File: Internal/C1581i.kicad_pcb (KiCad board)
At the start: 2 copper layers, 151.5 x 106.9 mm, 71 parts, among them CN1 FLOPPY POWER, CN2 FLOPPY, CN5 LEDS, CN7 INTERNAL IEC, CN8 EXTERNAL POWER, J1 PIN34, J2 PIN2, J3 DRIVE SELECT, J5 ROM SELECT, J90 Barrel_Jack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

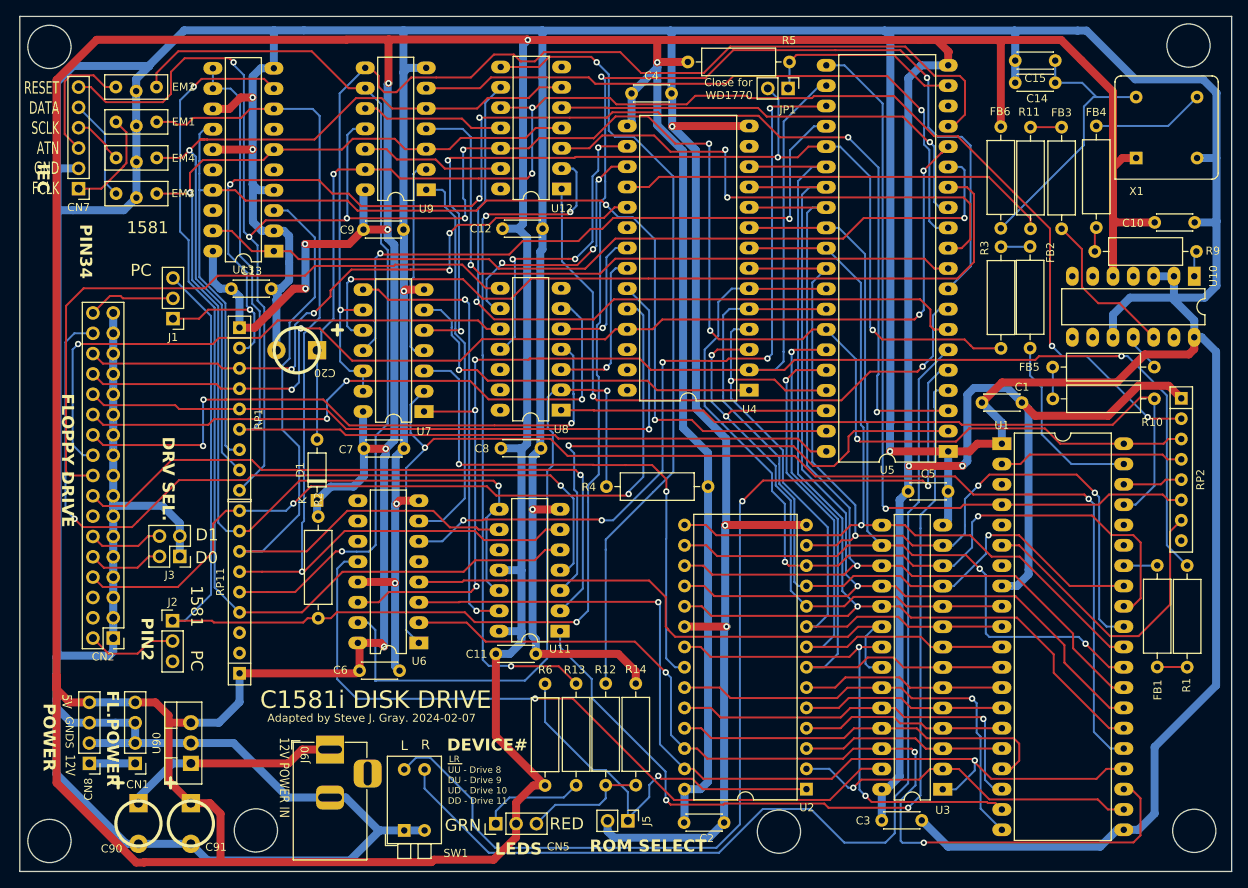
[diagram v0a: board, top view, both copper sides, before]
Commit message: 1581i Update
Lots of re-routing to pack components tighter. PCB is now smaller. Added FPC connector to add Laptop PC drive support. Add board render.
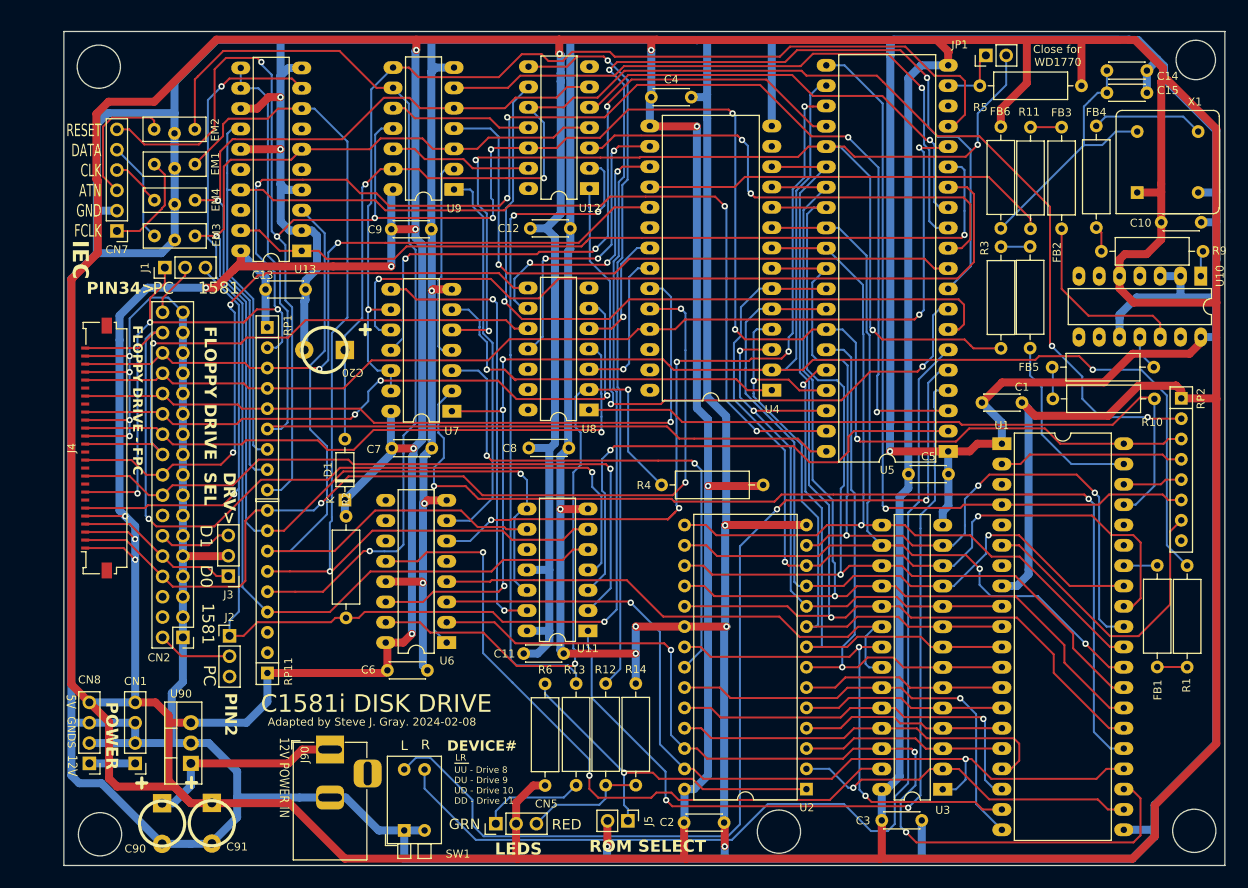
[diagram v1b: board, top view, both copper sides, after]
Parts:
- added J4: Conn_01x26, Connector_FFC-FPC:Molex_200528-0260_1x26-1MP_P1.00mm_Horizontal, F.Cu at (96.7, 89.9)
- J3: value DRIVE SELECT -> PIN2; footprint Connector_PinHeader_2.54mm:PinHeader_2x02_P2.54mm_Vertical -> Connector_PinHeader_2.54mm:PinHeader_1x03_P2.54mm_Vertical
- moved JP1 25.1 mm to (208.3, 40.8), turned to 90 degrees
- moved R5 24.0 mm to (207.6, 44.6), turned to 0 degrees
- moved CN2 8.71 mm to (108.0, 113.5)
- moved C15 7.61 mm to (223.5, 45.5), turned to 0 degrees
- moved J2 7.37 mm to (113.8, 113.3)
- moved CN7 7.14 mm to (99.7, 62.7)
- moved EM1 7.14 mm to (109.5, 54.4)
- moved EM4 7.14 mm to (109.5, 58.9)
- moved EM2 7.14 mm to (109.5, 50.0)
- moved EM3 7.14 mm to (109.5, 63.4)
- moved R4 6.89 mm to (167.8, 94.5)
- moved C14 6.64 mm to (223.5, 42.7), turned to 0 degrees
- moved J3 6.55 mm to (113.7, 105.9)
- moved J1 6.47 mm to (105.7, 67.3), turned to 90 degrees
- moved X1 4.31 mm to (227.3, 57.9)
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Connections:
- J3 pad 1: GND -> SELECT0
- J3 pad 2: SELECT0 -> GND
- J3 pad 3: GND -> SELECT1
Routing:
- net 5V: track 960.5 -> 1196.3 mm, vias 10 -> 13
- net GND: track 1108.0 -> 1220.9 mm, vias 10 -> 17
- net ~{RDY}: track 169.5 -> 212.8 mm, vias 6 -> 8
- net PHI2: track 127.3 -> 147.3 mm
- net Net-(JP1-A): track 25.2 -> 8.08 mm
- net ~{DISKCHANGE}: track 244.7 -> 261.7 mm, vias 3 -> 4
- net INDEX: track 100.8 -> 115.1 mm, vias 2 -> 3
- net SELECT0: track 9.47 -> 20.6 mm
- net Net-(R12-Pad2): track 99.3 -> 91.0 mm
- net ATN_IN: track 137.7 -> 130.2 mm
- net A3: track 74.7 -> 68.5 mm
- net READDATA: track 82.3 -> 88.3 mm, vias 4 -> 2
- net A14: track 116.5 -> 110.6 mm
- net SIDE0: track 70.9 -> 65.0 mm
- net ~{FLAG}: track 80.6 -> 86.4 mm, vias 2 -> 3
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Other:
- board size 151.5 x 106.9 mm -> 145.1 x 104.2 mm
- board text added: "Adapted by Steve J. Gray. 2024-02-08"
- board text added: "DRV> SEL"
- board text added: "FLOPPY DRIVE - FPC"
- board text added: "PIN34>"
- board text added: "RESET DATA CLK ATN GND FCLK"
- board text removed: "Adapted by Steve J. Gray. 2024-02-07"
- board text removed: "DRV SEL."
- board text removed: "FL.POWER"
- board text removed: "PIN34"
- board text removed: "RESET DATA SCLK ATN GND FCLK"

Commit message: Floppy connector area updates
Move floppy connector and jumpers. Add additional mounting holes.
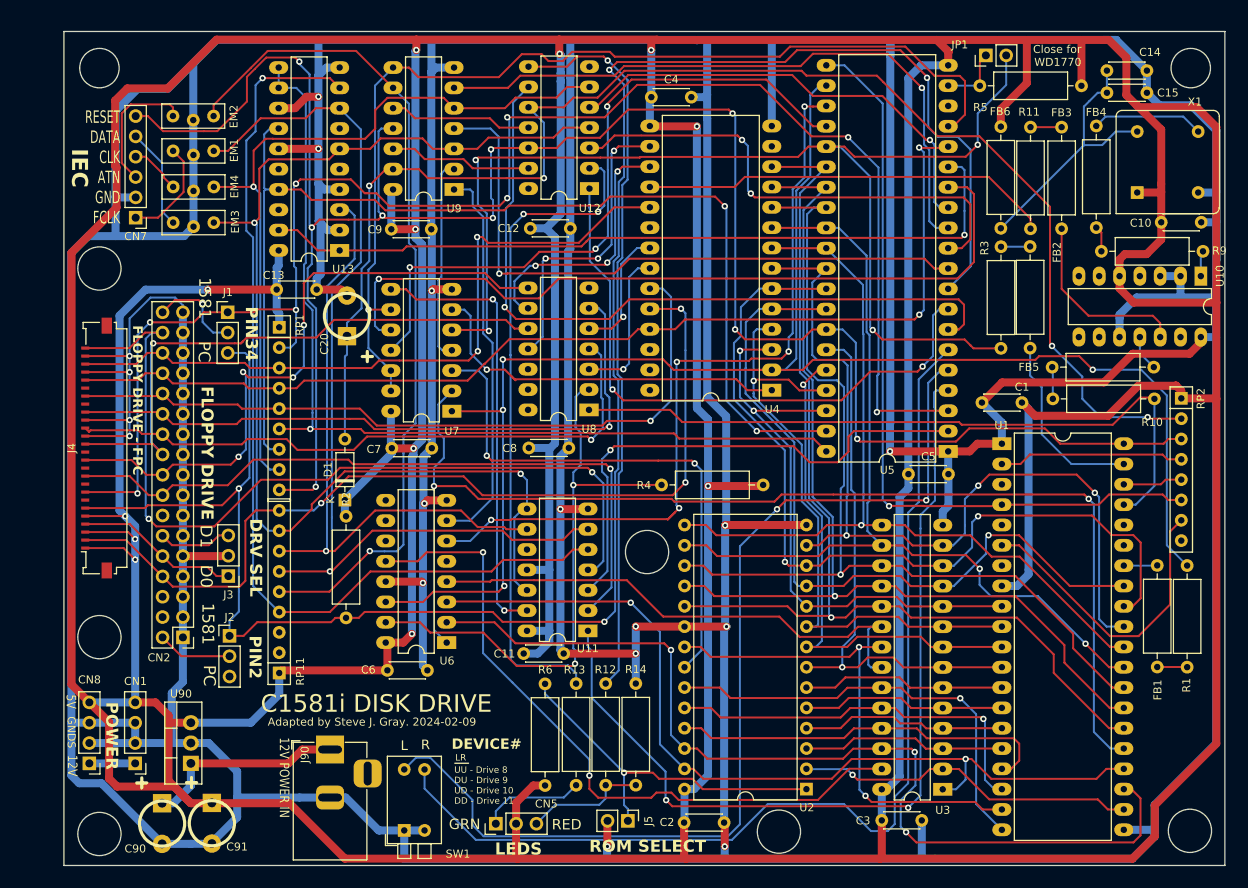
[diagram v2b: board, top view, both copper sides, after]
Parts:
- moved J1 9.65 mm to (113.6, 72.9), turned to 0 degrees
- moved C20 5.10 mm to (128.5, 73.3), turned to 90 degrees
- moved U13 4.74 mm to (127.6, 65.2)
- moved EM2 2.87 mm to (111.8, 48.4)
- moved EM1 2.87 mm to (111.8, 52.7)
- moved EM4 2.87 mm to (111.8, 57.2)
- moved CN7 2.87 mm to (102.1, 61.1)
- moved EM3 2.87 mm to (111.8, 61.7)
- moved RP1 1.49 mm to (120.0, 74.8)
- moved RP11 1.48 mm to (120.0, 118.0)
- moved C13 1.39 mm to (119.7, 70.1)
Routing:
- net GND: track 1220.9 -> 1190.2 mm
- net 5V: track 1196.3 -> 1171.1 mm, vias 13 -> 12
- net ~{DISKCHANGE}: track 261.7 -> 252.4 mm
- net ~{RDY}: track 212.8 -> 203.9 mm
- net Net-(U6B-E): track 80.8 -> 73.2 mm
- net ~{ATN}: track 112.8 -> 105.4 mm
- net READDATA: track 88.3 -> 94.6 mm
- net Net-(RP11F-R6.2): track 85.7 -> 79.6 mm, vias 0 -> 1
- net SP: track 147.1 -> 141.3 mm
- net FAST_SER_DIR: track 103.5 -> 97.9 mm
- net FD_PIN34: track 6.76 -> 11.8 mm, vias 0 -> 1
- net DATA: track 152.5 -> 147.6 mm
- net CNT: track 122.2 -> 118.1 mm, vias 0 -> 1
- net ~{RESET}: track 265.8 -> 261.9 mm, vias 8 -> 9
- net Net-(RP11C-R3.2): track 123.7 -> 121.2 mm
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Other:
- outline, holes or cut-outs redrawn
- board text added: "Adapted by Steve J. Gray. 2024-02-09"
- board text added: "DRV SEL"
- board text added: "PIN34"
- board text removed: "Adapted by Steve J. Gray. 2024-02-08"
- board text removed: "DRV> SEL"
- board text removed: "PIN34>"

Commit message: Add Enable/Disable Jumper
Allows use of an external switch to enable/disable the drive.
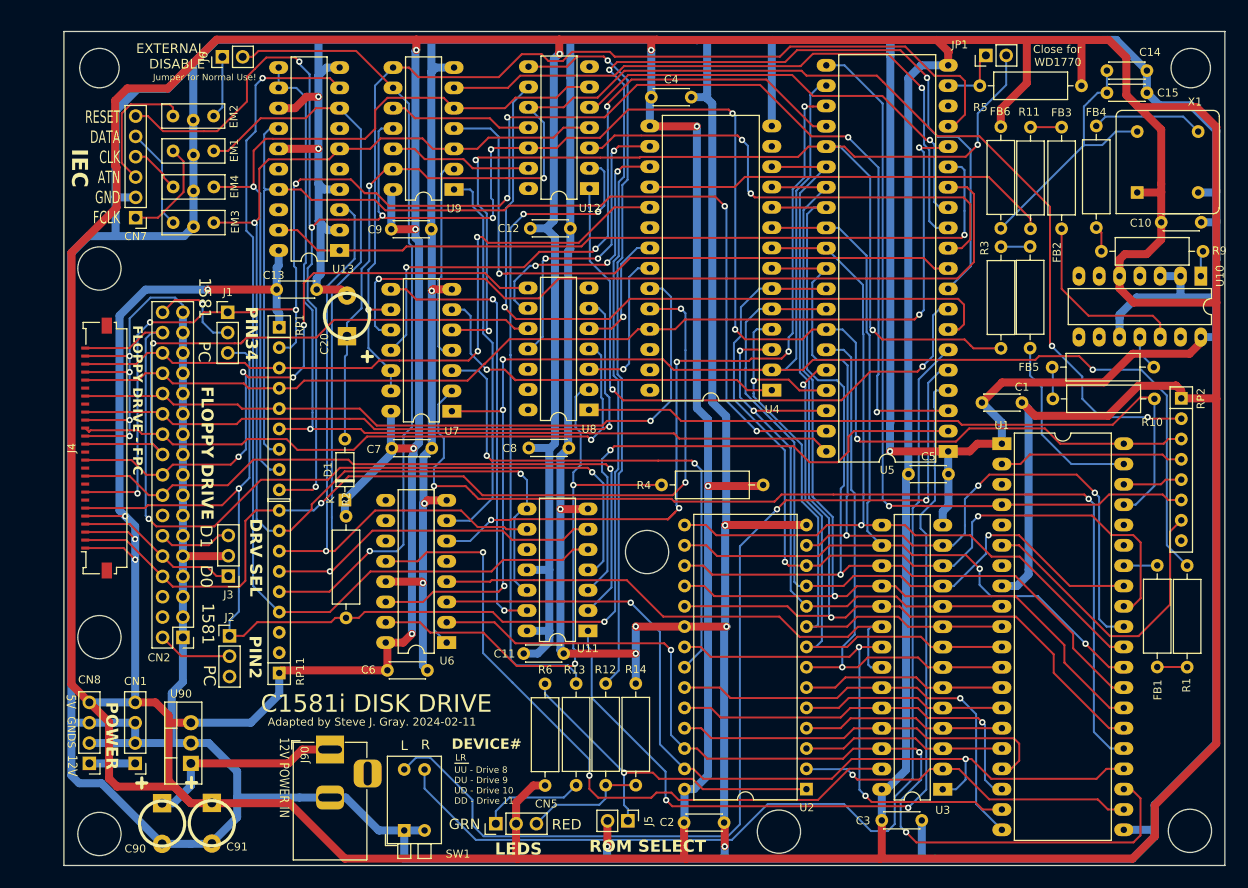
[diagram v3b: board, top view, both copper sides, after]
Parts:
- added J6: DRIVE ENABLE, Connector_PinHeader_2.54mm:PinHeader_1x02_P2.54mm_Vertical, F.Cu at (112.9, 41.0)
- J4: value Conn_01x26 -> FPC
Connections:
- EM2 pad 1: ~{ATN} -> Net-(J6-Pin_1)
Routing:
- net ~{ATN}: track 105.4 -> 97.6 mm
- net Net-(J6-Pin_1): track 0.00 -> 7.85 mm
- net A13: track 121.0 -> 121.9 mm
- net ~{MOTOR}: track 111.1 -> 111.7 mm
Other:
- board text added: "Adapted by Steve J. Gray. 2024-02-11"
- board text added: "EXTERNAL DISABLE"
- board text added: "Jumper for Normal Use!"
- board text removed: "Adapted by Steve J. Gray. 2024-02-09"

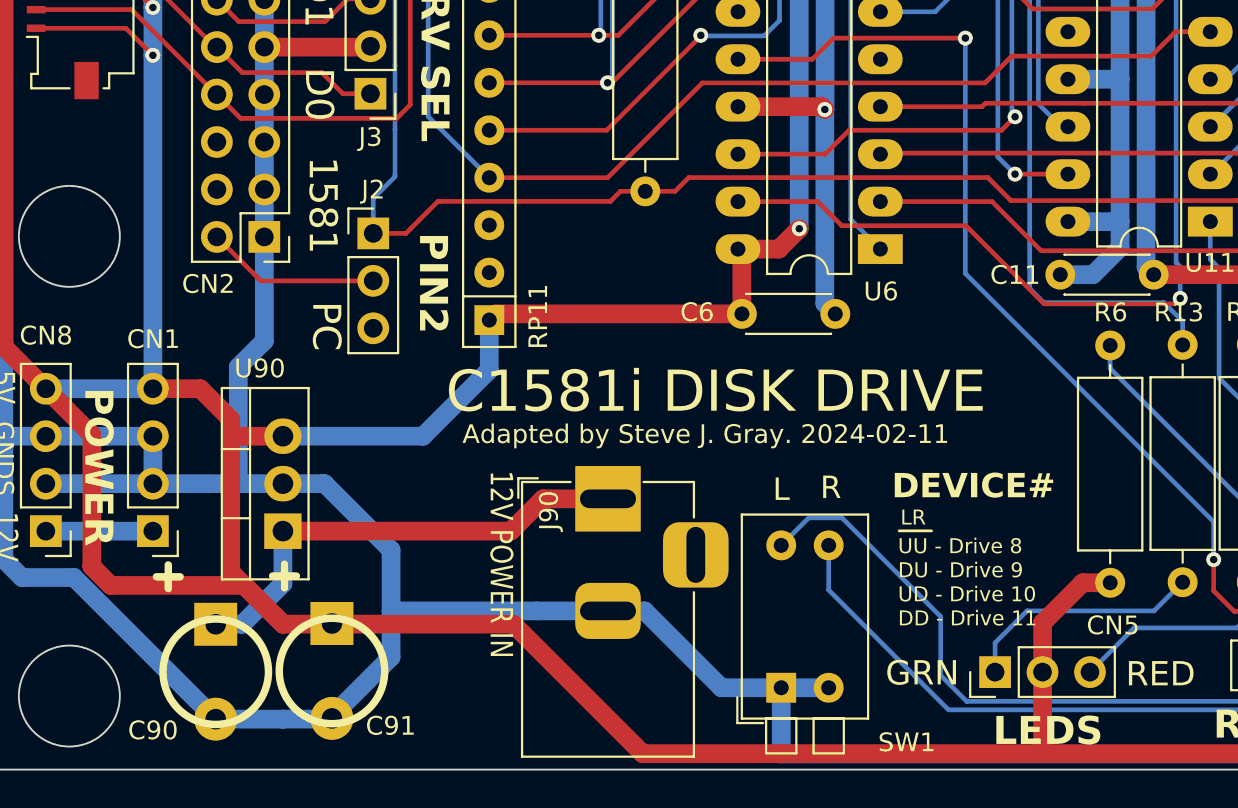
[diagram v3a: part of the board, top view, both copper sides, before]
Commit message: 1581i - Fix 12v power
Fix 12V from barrel jack not connecting to floppy power. I am making  a small run of boards from JLCPCB to test the design.
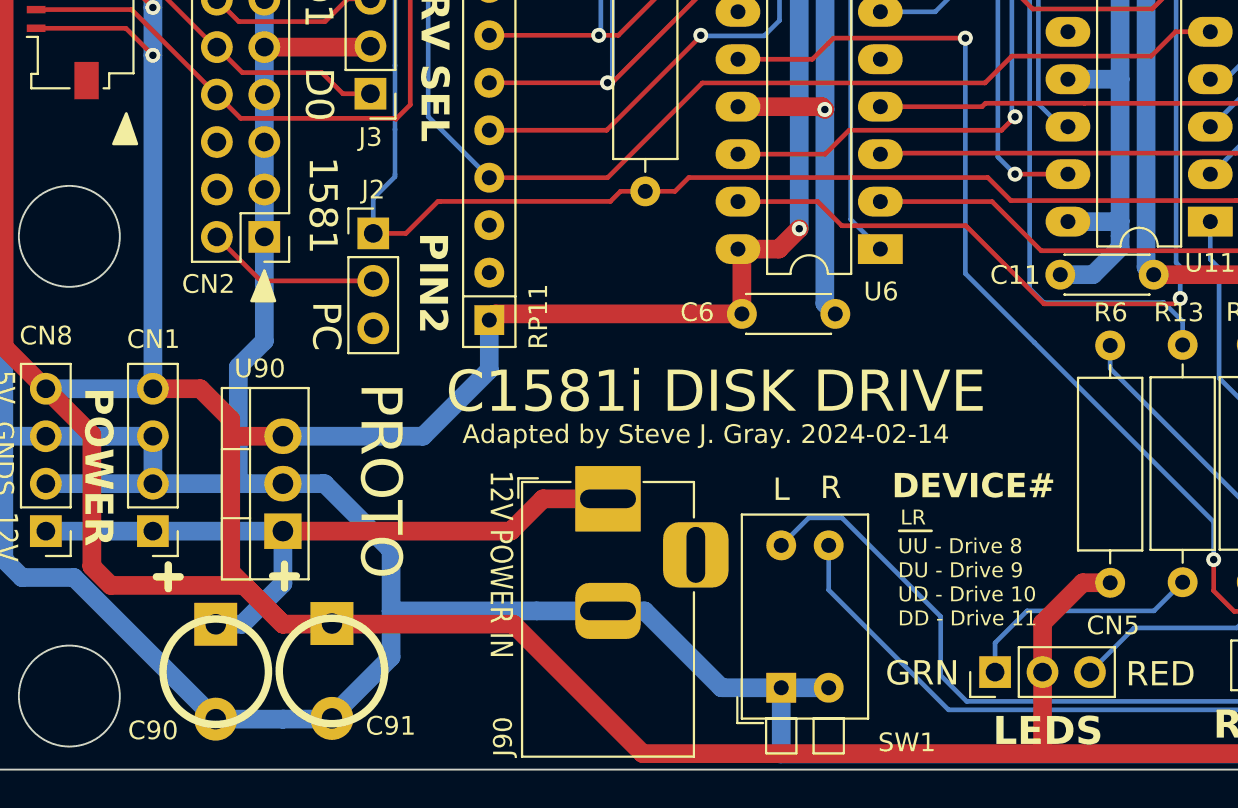
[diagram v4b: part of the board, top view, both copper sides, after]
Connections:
- C90 pad 1: 12VIN -> 12V
- J90 pad 1: 12VIN -> 12V
- U90 pad 1: 12VIN -> 12V
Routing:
- net 12V: track 5.73 -> 38.1 mm
- net 12VIN: track 25.4 -> 0.00 mm
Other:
- board text added: "Adapted by Steve J. Gray. 2024-02-14"
- board text added: "PROTO"
- board text removed: "Adapted by Steve J. Gray. 2024-02-11"
